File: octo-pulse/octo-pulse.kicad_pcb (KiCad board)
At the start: 2 copper layers, 56 x 59 mm, 8 parts, among them SW1 SW_Push, SW2 SW_Push, SW3 SW_Push, SW4 SW_Push, SW5 SW_Push, SW6 SW_Push

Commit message: Fully wired PCB in KiCad
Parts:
- removed A1: RaspberryPi_Pico, Module:RaspberryPi_Pico_Common_Unspecified
- added U1: XIAO-RP2040-NORMAL, Seeed Studio XIAO Series Library:XIAO-RP2040-DIP, B.Cu at (166.0, 112.4)
- SSD1306:128x64OLED1: footprint SSD1306:128x64OLED -> SSD1306:Adafruit_SSD1306_1.3''
- SW1: value SW_Push -> SW_TL
- SW2: value SW_Push -> SW_TR
- SW3: value SW_Push -> SW_ML
- SW4: value SW_Push -> SW_MR
- SW5: value SW_Push -> SW_BL
- SW6: value SW_Push -> SW_BR
- moved SSD1306:128x64OLED1 15.1 mm to (156.6, 75.0)
- moved SW6 5.00 mm to (189.0, 100.0)
- moved SW5 4.47 mm to (142.0, 100.0)
- moved SW2 4.27 mm to (189.0, 71.0)
- moved SW4 4.24 mm to (189.0, 87.0)
- moved SW3 3.61 mm to (142.0, 87.0)
- moved SW1 3.59 mm to (142.0, 71.0)
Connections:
- SSD1306:128x64OLED1 pad 3: A4 -> SCL
- SSD1306:128x64OLED1 pad 4: A5 -> SDA
- SW1 pad 1: unconnected-(SW1-Pad1) -> VCC
- SW2 pad 1: unconnected-(SW2-Pad1) -> VCC
- SW3 pad 1: unconnected-(SW3-Pad1) -> VCC
- SW4 pad 1: unconnected-(SW4-Pad1) -> VCC
- SW5 pad 1: unconnected-(SW5-Pad1) -> VCC
- SW6 pad 1: unconnected-(SW6-Pad1) -> VCC
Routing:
- net VCC: track 0.00 -> 175.3 mm, vias 0 -> 1
- net Net-(U1-GPIO27/ADC1/A1): track 0.00 -> 74.9 mm
- net Net-(U1-GPIO29/ADC3/A3): track 0.00 -> 70.5 mm
- net Net-(U1-GPIO26/ADC0/A0): track 0.00 -> 58.0 mm
- net SDA: track 0.00 -> 50.8 mm
- net GND: track 0.00 -> 49.5 mm
- net Net-(U1-GPIO1/RX): track 0.00 -> 47.9 mm, vias 0 -> 1
- net SCL: track 0.00 -> 42.6 mm
- net Net-(U1-GPIO28/ADC2/A2): track 0.00 -> 35.8 mm
- net Net-(U1-GPIO2/SCK): track 0.00 -> 22.6 mm
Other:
- board size 56 x 59 mm -> 61 x 54 mm

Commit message: Finished & decorated PCB, onto programming!
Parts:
- added G***: LOGO, LOGO, B.Cu at (166.0, 97.0)
- U1: moved to F.Cu
- turned U1 to 180 degrees
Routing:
- net Net-(U1-GPIO28/ADC2/A2): track 35.8 -> 65.3 mm
- net Net-(U1-GPIO29/ADC3/A3): track 70.5 -> 44.3 mm
- net Net-(U1-GPIO2/SCK): track 22.6 -> 47.8 mm
- net Net-(U1-GPIO27/ADC1/A1): track 74.9 -> 55.4 mm
- net Net-(U1-GPIO1/RX): track 47.9 -> 29.0 mm
- net Net-(U1-GPIO26/ADC0/A0): track 58.0 -> 74.7 mm
- net SDA: track 50.8 -> 38.7 mm
- net VCC: track 175.3 -> 166.6 mm, vias 1 -> 2
- net GND: track 49.5 -> 47.0 mm
- net SCL: track 42.6 -> 42.0 mm

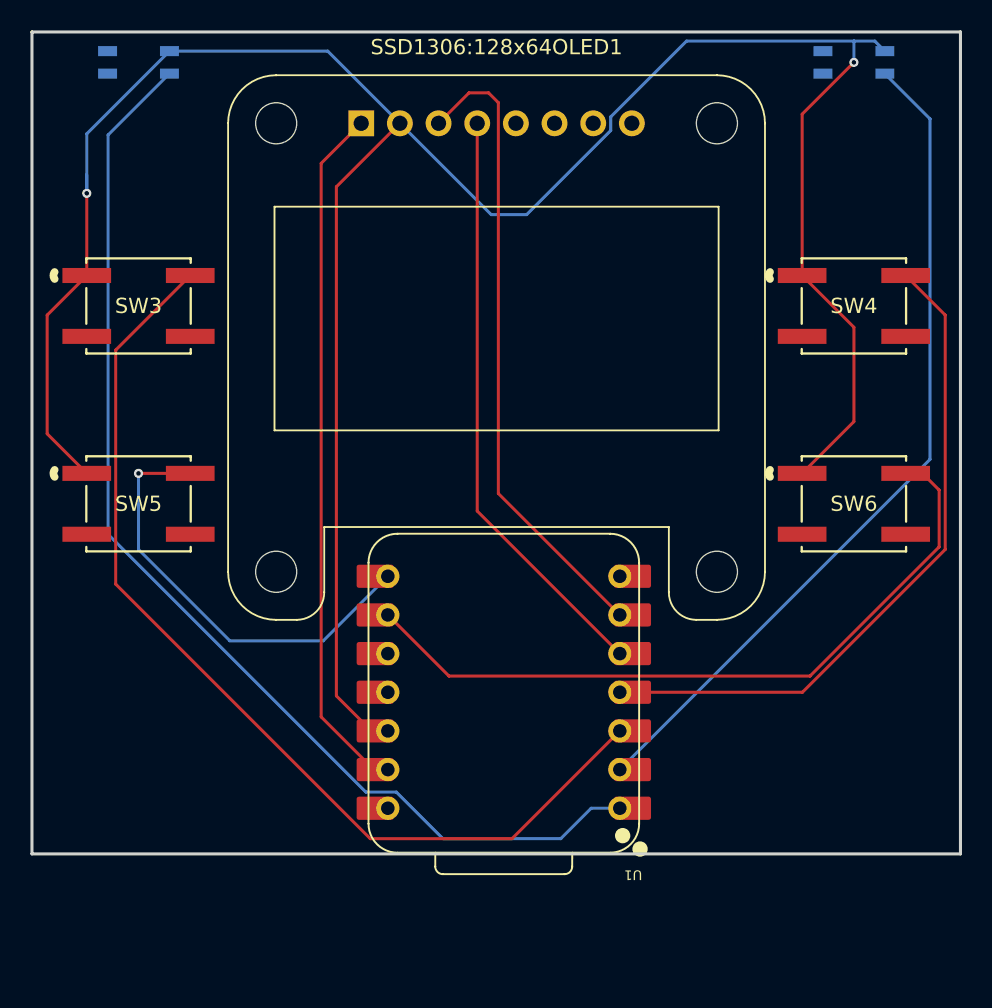
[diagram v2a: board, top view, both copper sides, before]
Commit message: replaced switches on PCB with new ones: B3U-1000P & B3U-3000P-B
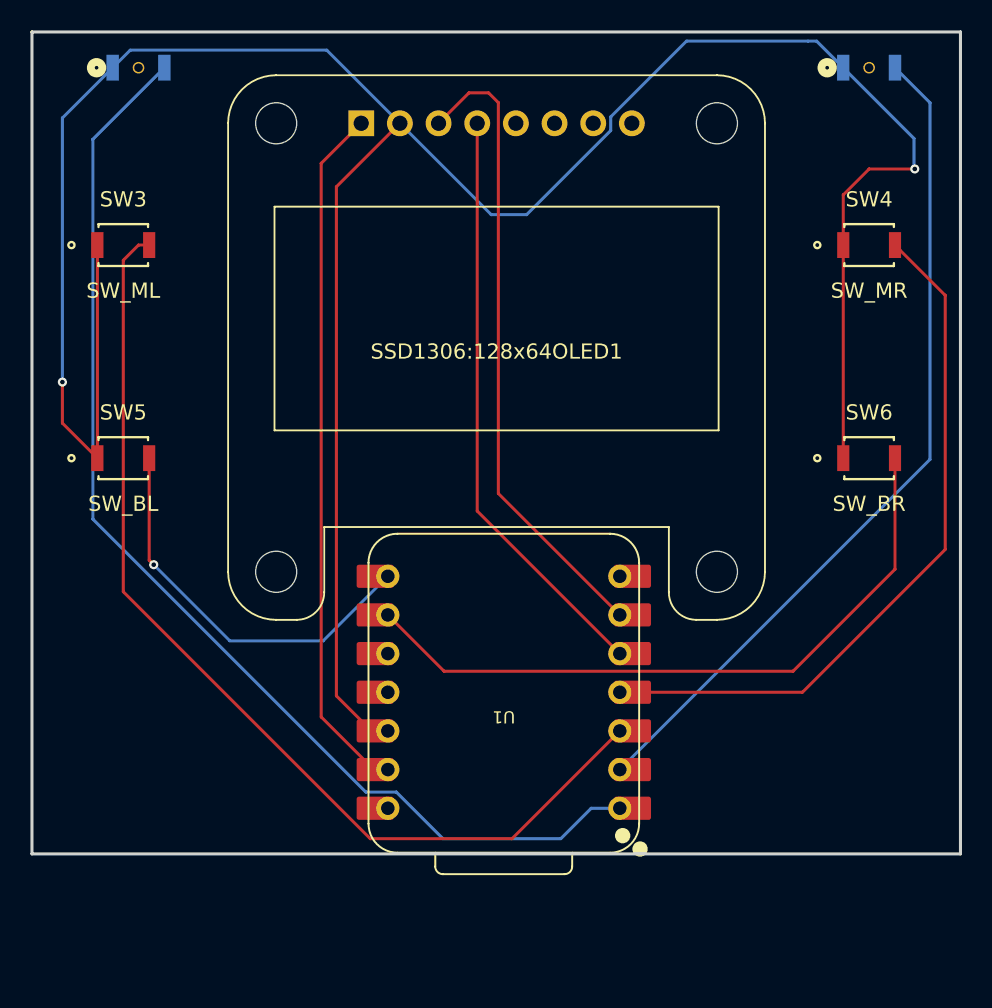
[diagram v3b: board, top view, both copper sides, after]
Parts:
- SW1, SW2: footprint EVQ-P7A01P:EVQ_P7_PAN -> B3U-3000P-B:SW_B3U-3000P-B_OMR
- SW3, SW4, SW5, SW6: footprint EVQ-Q2K03W:EVQ-Q2K03W_PAN -> B3U-1000P:B3U-1000P
- moved SW3 4.12 mm to (141.0, 83.0)
- moved SW4 4.12 mm to (190.0, 83.0)
- moved SW5 3.16 mm to (141.0, 97.0)
- moved SW6 3.16 mm to (190.0, 97.0)
- moved SW2 1.00 mm to (190.0, 71.0)
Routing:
- net VCC: track 166.6 -> 175.9 mm
- net Net-(U1-GPIO2/SCK): track 47.8 -> 44.9 mm
- net Net-(U1-GPIO1/RX): track 29.0 -> 26.3 mm
- net Net-(U1-GPIO29/ADC3/A3): track 44.3 -> 46.6 mm
- net Net-(U1-GPIO26/ADC0/A0): track 74.7 -> 75.7 mm
- net Net-(U1-GPIO28/ADC2/A2): track 65.3 -> 66.2 mm
